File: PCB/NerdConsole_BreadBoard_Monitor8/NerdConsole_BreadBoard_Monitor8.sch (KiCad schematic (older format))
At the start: 11 parts, among them J1 Conn_01x09, J2 Conn_01x09

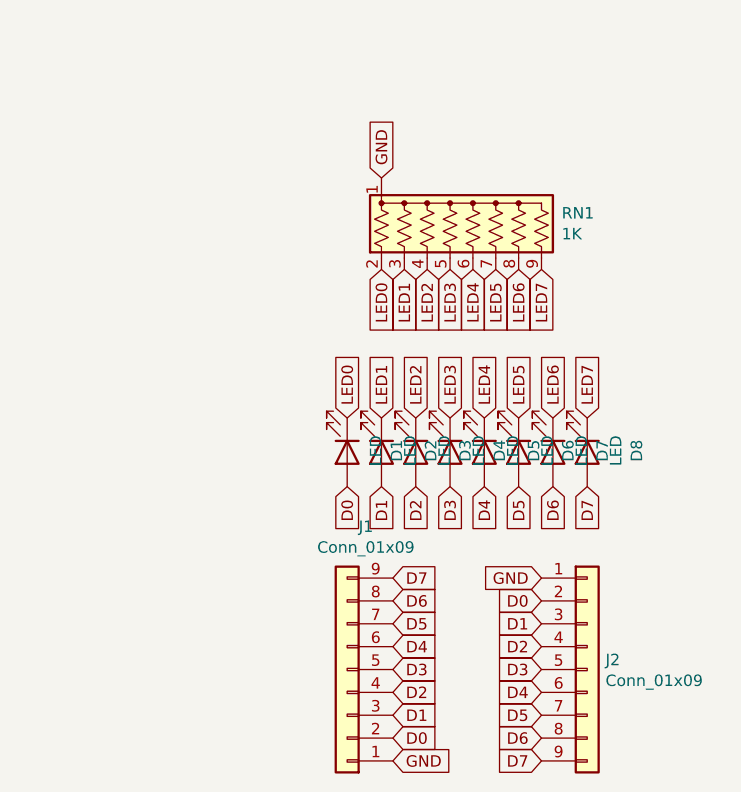
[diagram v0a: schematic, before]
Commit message: Renamed Monitor to BridgeMonitor and made a new free standing Monitor.
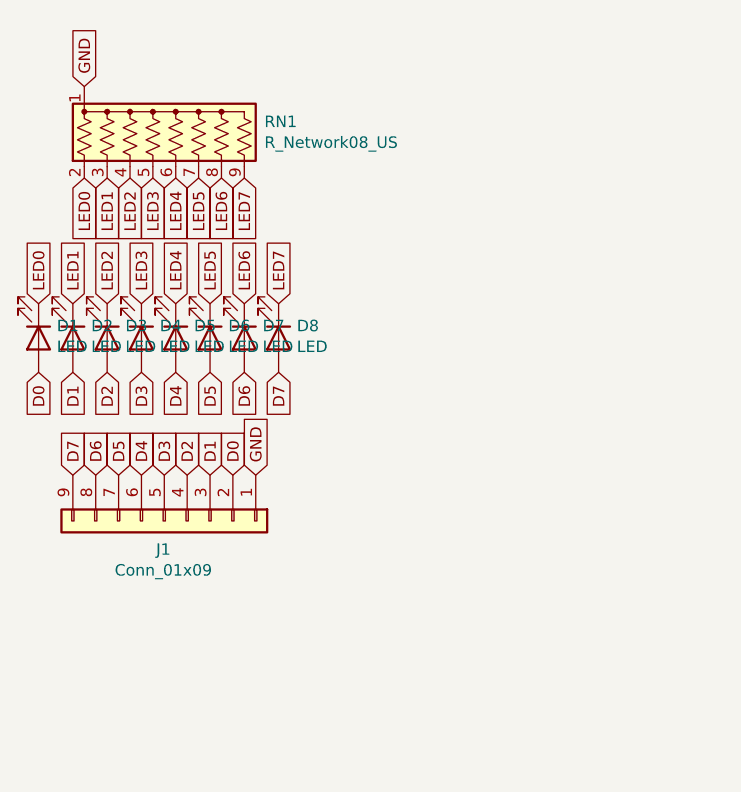
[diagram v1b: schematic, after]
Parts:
- removed J2: Conn_01x09, Connector_PinHeader_2.54mm:PinHeader_1x09_P2.54mm_Vertical, symbol Connector_Generic:Conn_01x09
- J1: footprint Connector_PinHeader_2.54mm:PinHeader_1x09_P2.54mm_Vertical -> Connector_PinSocket_2.54mm:PinSocket_1x09_P2.54mm_Vertical
- RN1: value 1K -> R_Network08_US
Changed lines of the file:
@@
 $EndDescr
 $Comp
-L Connector_Generic:Conn_01x09 J2
-U 1 1 601BF5DC
-P 6450 4400
-F 0 "J2" H 6530 4442 50  0000 L CNN
-F 1 "Conn_01x09" H 6530 4351 50  0000 L CNN
-F 2 "Connector_PinHeader_2.54mm:PinHeader_1x09_P2.54mm_Vertical" H 6450 4400 50  0001 C CNN
-F 3 "~" H 6450 4400 50  0001 C CNN
-	1    6450 4400
+L Device:R_Network08_US RN1
+U 1 1 601B6E15
+P 4650 2050
+F 0 "RN1" H 5038 2096 50  0000 L CNN
+F 1 "R_Network08_US" H 5038 2005 50  0000 L CNN
+F 2 "Resistor_THT:R_Array_SIP9" V 5125 2050 50  0001 C CNN
+F 3 "http://www.vishay.com/docs/31509/csc.pdf" H 4650 2050 50  0001 C CNN
+	1    4650 2050
 	1    0    0    -1
 $EndComp
 $Comp
-L Connector_Generic:Conn_01x09 J1
-U 1 1 601BFF2C
-P 5400 4400
-F 0 "J1" H 5318 3775 50  0000 C CNN
-F 1 "Conn_01x09" H 5318 3866 50  0000 C CNN
-F 2 "Connector_PinHeader_2.54mm:PinHeader_1x09_P2.54mm_Vertical" H 5400 4400 50  0001 C CNN
-F 3 "~" H 5400 4400 50  0001 C CNN
-	1    5400 4400
-	-1   0    0    1
-$EndComp
-Text GLabel 6250 4100 0    50   Input ~ 0
-D0
-Text GLabel 6250 4200 0    50   Input ~ 0
-D1
-Text GLabel 6250 4300 0    50   Input ~ 0
-D2
-Text GLabel 6250 4400 0    50   Input ~ 0
-D3
-Text GLabel 6250 4500 0    50   Input ~ 0
-D4
-Text GLabel 6250 4600 0    50   Input ~ 0
-D5
-Text GLabel 6250 4700 0    50   Input ~ 0
-D6
-Text GLabel 6250 4800 0    50   Input ~ 0
-D7
-Text GLabel 6250 4000 0    50   Input ~ 0
-GND
-Text GLabel 5600 4800 2    50   Input ~ 0
-GND
-$Comp
-L Device:R_Network08_US RN1
-U 1 1 601C2C63
-P 5950 2450
-F 0 "RN1" H 6338 2496 50  0000 L CNN
-F 1 "1K" H 6338 2405 50  0000 L CNN
-F 2 "Resistor_THT:R_Array_SIP9" V 6425 2450 50  0001 C CNN
-F 3 "http://www.vishay.com/docs/31509/csc.pdf" H 5950 2450 50  0001 C CNN
-	1    5950 2450
-	1    0    0    -1
+L Device:LED D1
+U 1 1 601B764C
+P 4050 2950
+F 0 "D1" V 3997 3030 50  0000 L CNN
+F 1 "LED" V 4088 3030 50  0000 L CNN
+F 2 "LED_SMD:LED_0805_2012Metric_Pad1.15x1.40mm_HandSolder" H 4050 2950 50  0001 C CNN
+F 3 "~" H 4050 2950 50  0001 C CNN
+	1    4050 2950
+	0    1    1    0
 $EndComp
 $Comp
-L Device:LED D8
-U 1 1 601C6EE7
-P 6450 3450
-F 0 "D8" H 6443 3667 50  0000 C CNN
-F 1 "LED" H 6443 3576 50  0000 C CNN
-F 2 "LED_SMD:LED_0805_2012Metric_Pad1.15x1.40mm_HandSolder" H 6450 3450 50  0001 C CNN
-F 3 "~" H 6450 3450 50  0001 C CNN
-	1    6450 3450
+L Device:LED D2
+U 1 1 601B7942
+P 4200 2950
+F 0 "D2" V 4147 3030 50  0000 L CNN
+F 1 "LED" V 4238 3030 50  0000 L CNN
+F 2 "LED_SMD:LED_0805_2012Metric_Pad1.15x1.40mm_HandSolder" H 4200 2950 50  0001 C CNN
+F 3 "~" H 4200 2950 50  0001 C CNN
+	1    4200 2950
+	0    1    1    0
+$EndComp
+$Comp
+L Device:LED D3
+U 1 1 601B8D13
+P 4350 2950
+F 0 "D3" V 4297 3030 50  0000 L CNN
+F 1 "LED" V 4388 3030 50  0000 L CNN
+F 2 "LED_SMD:LED_0805_2012Metric_Pad1.15x1.40mm_HandSolder" H 4350 2950 50  0001 C CNN
+F 3 "~" H 4350 2950 50  0001 C CNN
+	1    4350 2950
+	0    1    1    0
+$EndComp
+$Comp
+L Device:LED D4
+U 1 1 601B8D19
+P 4500 2950
+F 0 "D4" V 4447 3030 50  0000 L CNN
+F 1 "LED" V 4538 3030 50  0000 L CNN
+F 2 "LED_SMD:LED_0805_2012Metric_Pad1.15x1.40mm_HandSolder" H 4500 2950 50  0001 C CNN
+F 3 "~" H 4500 2950 50  0001 C CNN
+	1    4500 2950
+	0    1    1    0
+$EndComp
+$Comp
+L Device:LED D5
+U 1 1 601BA12B
+P 4650 2950
+F 0 "D5" V 4597 3030 50  0000 L CNN
+F 1 "LED" V 4688 3030 50  0000 L CNN
+F 2 "LED_SMD:LED_0805_2012Metric_Pad1.15x1.40mm_HandSolder" H 4650 2950 50  0001 C CNN
+F 3 "~" H 4650 2950 50  0001 C CNN
+	1    4650 2950
+	0    1    1    0
+$EndComp
+$Comp
+L Device:LED D6
+U 1 1 601BA131
+P 4800 2950
+F 0 "D6" V 4747 3030 50  0000 L CNN
+F 1 "LED" V 4838 3030 50  0000 L CNN
+F 2 "LED_SMD:LED_0805_2012Metric_Pad1.15x1.40mm_HandSolder" H 4800 2950 50  0001 C CNN
+F 3 "~" H 4800 2950 50  0001 C CNN
+	1    4800 2950
 	0    1    1    0
 $EndComp
 $Comp
 L Device:LED D7
-U 1 1 601C7509
-P 6300 3450
-F 0 "D7" H 6293 3667 50  0000 C CNN
-F 1 "LED" H 6293 3576 50  0000 C CNN
-F 2 "LED_SMD:LED_0805_2012Metric_Pad1.15x1.40mm_HandSolder" H 6300 3450 50  0001 C CNN
-F 3 "~" H 6300 3450 50  0001 C CNN
-	1    6300 3450
+U 1 1 601BA137
+P 4950 2950
+F 0 "D7" V 4897 3030 50  0000 L CNN
+F 1 "LED" V 4988 3030 50  0000 L CNN
+F 2 "LED_SMD:LED_0805_2012Metric_Pad1.15x1.40mm_HandSolder" H 4950 2950 50  0001 C CNN
+F 3 "~" H 4950 2950 50  0001 C CNN
+	1    4950 2950
 	0    1    1    0
 $EndComp
 $Comp
-L Device:LED D6
-U 1 1 601C8500
-P 6150 3450
-F 0 "D6" H 6143 3667 50  0000 C CNN
-F 1 "LED" H 6143 3576 50  0000 C CNN
-F 2 "LED_SMD:LED_0805_2012Metric_Pad1.15x1.40mm_HandSolder" H 6150 3450 50  0001 C CNN
-F 3 "~" H 6150 3450 50  0001 C CNN
-	1    6150 3450
+L Device:LED D8
+U 1 1 601BA13D
+P 5100 2950
+F 0 "D8" V 5047 3030 50  0000 L CNN
+F 1 "LED" V 5138 3030 50  0000 L CNN
+F 2 "LED_SMD:LED_0805_2012Metric_Pad1.15x1.40mm_HandSolder" H 5100 2950 50  0001 C CNN
+F 3 "~" H 5100 2950 50  0001 C CNN
+	1    5100 2950
 	0    1    1    0
 $EndComp
 $Comp
-L Device:LED D5
-U 1 1 601C8506
-P 6000 3450
-F 0 "D5" H 5993 3667 50  0000 C CNN
-F 1 "LED" H 5993 3576 50  0000 C CNN
-F 2 "LED_SMD:LED_0805_2012Metric_Pad1.15x1.40mm_HandSolder" H 6000 3450 50  0001 C CNN
-F 3 "~" H 6000 3450 50  0001 C CNN
-	1    6000 3450
+L Connector_Generic:Conn_01x09 J1
+U 1 1 601BF4EB
+P 4600 3750
+F 0 "J1" V 4725 3746 50  0000 C CNN
+F 1 "Conn_01x09" V 4816 3746 50  0000 C CNN
+F 2 "Connector_PinSocket_2.54mm:PinSocket_1x09_P2.54mm_Vertical" H 4600 3750 50  0001 C CNN
+F 3 "~" H 4600 3750 50  0001 C CNN
+	1    4600 3750
 	0    1    1    0
 $EndComp
-$Comp
-L Device:LED D4
-U 1 1 601C8D8A
-P 5850 3450
-F 0 "D4" H 5843 3667 50  0000 C CNN
-F 1 "LED" H 5843 3576 50  0000 C CNN
-F 2 "LED_SMD:LED_0805_2012Metric_Pad1.15x1.40mm_HandSolder" H 5850 3450 50  0001 C CNN
-F 3 "~" H 5850 3450 50  0001 C CNN
-	1    5850 3450
-	0    1    1    0
-$EndComp
-$Comp
-L Device:LED D3
-U 1 1 601C8D90
-P 5700 3450
-F 0 "D3" H 5693 3667 50  0000 C CNN
-F 1 "LED" H 5693 3576 50  0000 C CNN
-F 2 "LED_SMD:LED_0805_2012Metric_Pad1.15x1.40mm_HandSolder" H 5700 3450 50  0001 C CNN
-F 3 "~" H 5700 3450 50  0001 C CNN
-	1    5700 3450
-	0    1    1    0
-$EndComp
-$Comp
-L Device:LED D2
-U 1 1 601C98D4
-P 5550 3450
-F 0 "D2" H 5543 3667 50  0000 C CNN
-F 1 "LED" H 5543 3576 50  0000 C CNN
-F 2 "LED_SMD:LED_0805_2012Metric_Pad1.15x1.40mm_HandSolder" H 5550 3450 50  0001 C CNN
-F 3 "~" H 5550 3450 50  0001 C CNN
-	1    5550 3450
-	0    1    1    0
-$EndComp
-$Comp
-L Device:LED D1
-U 1 1 601C98DA
-P 5400 3450
-F 0 "D1" H 5393 3667 50  0000 C CNN
-F 1 "LED" H 5393 3576 50  0000 C CNN
-F 2 "LED_SMD:LED_0805_2012Metric_Pad1.15x1.40mm_HandSolder" H 5400 3450 50  0001 C CNN
-F 3 "~" H 5400 3450 50  0001 C CNN
-	1    5400 3450
-	0    1    1    0
-$EndComp
-Text GLabel 5550 2250 1    50   Input ~ 0
+Text GLabel 5000 3550 1    50   Input ~ 0
 GND
-Text GLabel 5400 3600 3    50   Input ~ 0
+Text GLabel 4900 3550 1    50   Input ~ 0
 D0
-Text GLabel 5550 3600 3    50   Input ~ 0
+Text GLabel 4800 3550 1    50   Input ~ 0
 D1
-Text GLabel 5700 3600 3    50   Input ~ 0
+Text GLabel 4700 3550 1    50   Input ~ 0
 D2
-Text GLabel 5850 3600 3    50   Input ~ 0
+Text GLabel 4600 3550 1    50   Input ~ 0
 D3
-Text GLabel 6000 3600 3    50   Input ~ 0
+Text GLabel 4500 3550 1    50   Input ~ 0
 D4
-Text GLabel 6150 3600 3    50   Input ~ 0
+Text GLabel 4400 3550 1    50   Input ~ 0
 D5
-Text GLabel 6300 3600 3    50   Input ~ 0
+Text GLabel 4300 3550 1    50   Input ~ 0
 D6
-Text GLabel 6450 3600 3    50   Input ~ 0
+Text GLabel 4200 3550 1    50   Input ~ 0
 D7
-Text GLabel 5400 3300 1    50   Input ~ 0
+Text GLabel 4250 1850 1    50   Input ~ 0
+GND
+Text GLabel 4250 2250 3    50   Input ~ 0
 LED0
-Text GLabel 5550 3300 1    50   Input ~ 0
+Text GLabel 4350 2250 3    50   Input ~ 0
 LED1
-Text GLabel 5700 3300 1    50   Input ~ 0
+Text GLabel 4450 2250 3    50   Input ~ 0
 LED2
-Text GLabel 5850 3300 1    50   Input ~ 0
+Text GLabel 4550 2250 3    50   Input ~ 0
 LED3
-Text GLabel 6000 3300 1    50   Input ~ 0
+Text GLabel 4650 2250 3    50   Input ~ 0
 LED4
-Text GLabel 6150 3300 1    50   Input ~ 0
+Text GLabel 4750 2250 3    50   Input ~ 0
 LED5
-Text GLabel 6300 3300 1    50   Input ~ 0
+Text GLabel 4850 2250 3    50   Input ~ 0
 LED6
-Text GLabel 6450 3300 1    50   Input ~ 0
+Text GLabel 4950 2250 3    50   Input ~ 0
 LED7
-Text GLabel 5550 2650 3    50   Input ~ 0
+Text GLabel 4050 2800 1    50   Input ~ 0
 LED0
-Text GLabel 5650 2650 3    50   Input ~ 0
+Text GLabel 4200 2800 1    50   Input ~ 0
 LED1
-Text GLabel 5750 2650 3    50   Input ~ 0
+Text GLabel 4350 2800 1    50   Input ~ 0
 LED2
-Text GLabel 5850 2650 3    50   Input ~ 0
+Text GLabel 4500 2800 1    50   Input ~ 0
 LED3
-Text GLabel 5950 2650 3    50   Input ~ 0
+Text GLabel 4650 2800 1    50   Input ~ 0
 LED4
-Text GLabel 6050 2650 3    50   Input ~ 0
+Text GLabel 4800 2800 1    50   Input ~ 0
 LED5
-Text GLabel 6150 2650 3    50   Input ~ 0
+Text GLabel 4950 2800 1    50   Input ~ 0
 LED6
-Text GLabel 6250 2650 3    50   Input ~ 0
+Text GLabel 5100 2800 1    50   Input ~ 0
 LED7
-Text GLabel 5600 4000 2    50   Input ~ 0
+Text GLabel 4050 3100 3    50   Input ~ 0
+D0
+Text GLabel 4200 3100 3    50   Input ~ 0
+D1
+Text GLabel 4350 3100 3    50   Input ~ 0
+D2
+Text GLabel 4500 3100 3    50   Input ~ 0
+D3
+Text GLabel 4650 3100 3    50   Input ~ 0
+D4
+Text GLabel 4800 3100 3    50   Input ~ 0
+D5
+Text GLabel 4950 3100 3    50   Input ~ 0
+D6
+Text GLabel 5100 3100 3    50   Input ~ 0
 D7
-Text GLabel 5600 4100 2    50   Input ~ 0
-D6
-Text GLabel 5600 4200 2    50   Input ~ 0
-D5
-Text GLabel 5600 4300 2    50   Input ~ 0
-D4
-Text GLabel 5600 4400 2    50   Input ~ 0
-D3
-Text GLabel 5600 4500 2    50   Input ~ 0
-D2
-Text GLabel 5600 4600 2    50   Input ~ 0
-D1
-Text GLabel 5600 4700 2    50   Input ~ 0
-D0
 $EndSCHEMATC
